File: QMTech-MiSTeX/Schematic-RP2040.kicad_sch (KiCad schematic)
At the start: 24 parts, among them J6 Conn_01x02, U3 W25Q128JVS, U4 RP2040, X1 X322512MSB4SI

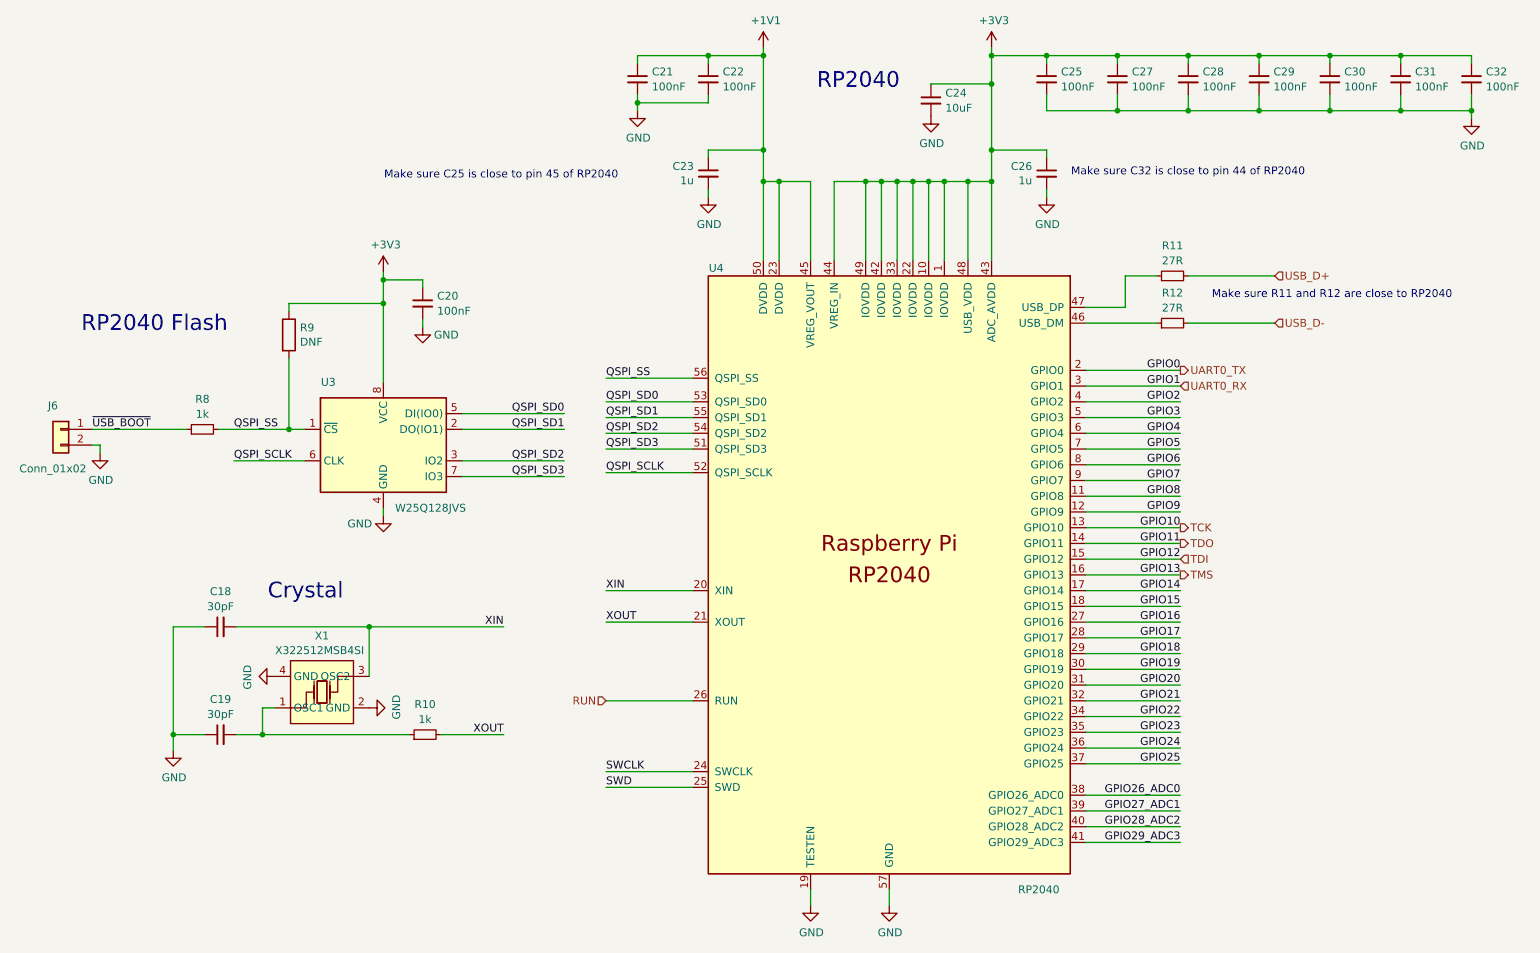
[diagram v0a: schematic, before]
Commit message: apply review notes from somhi, move audio into its own subsheet, add analog audio out
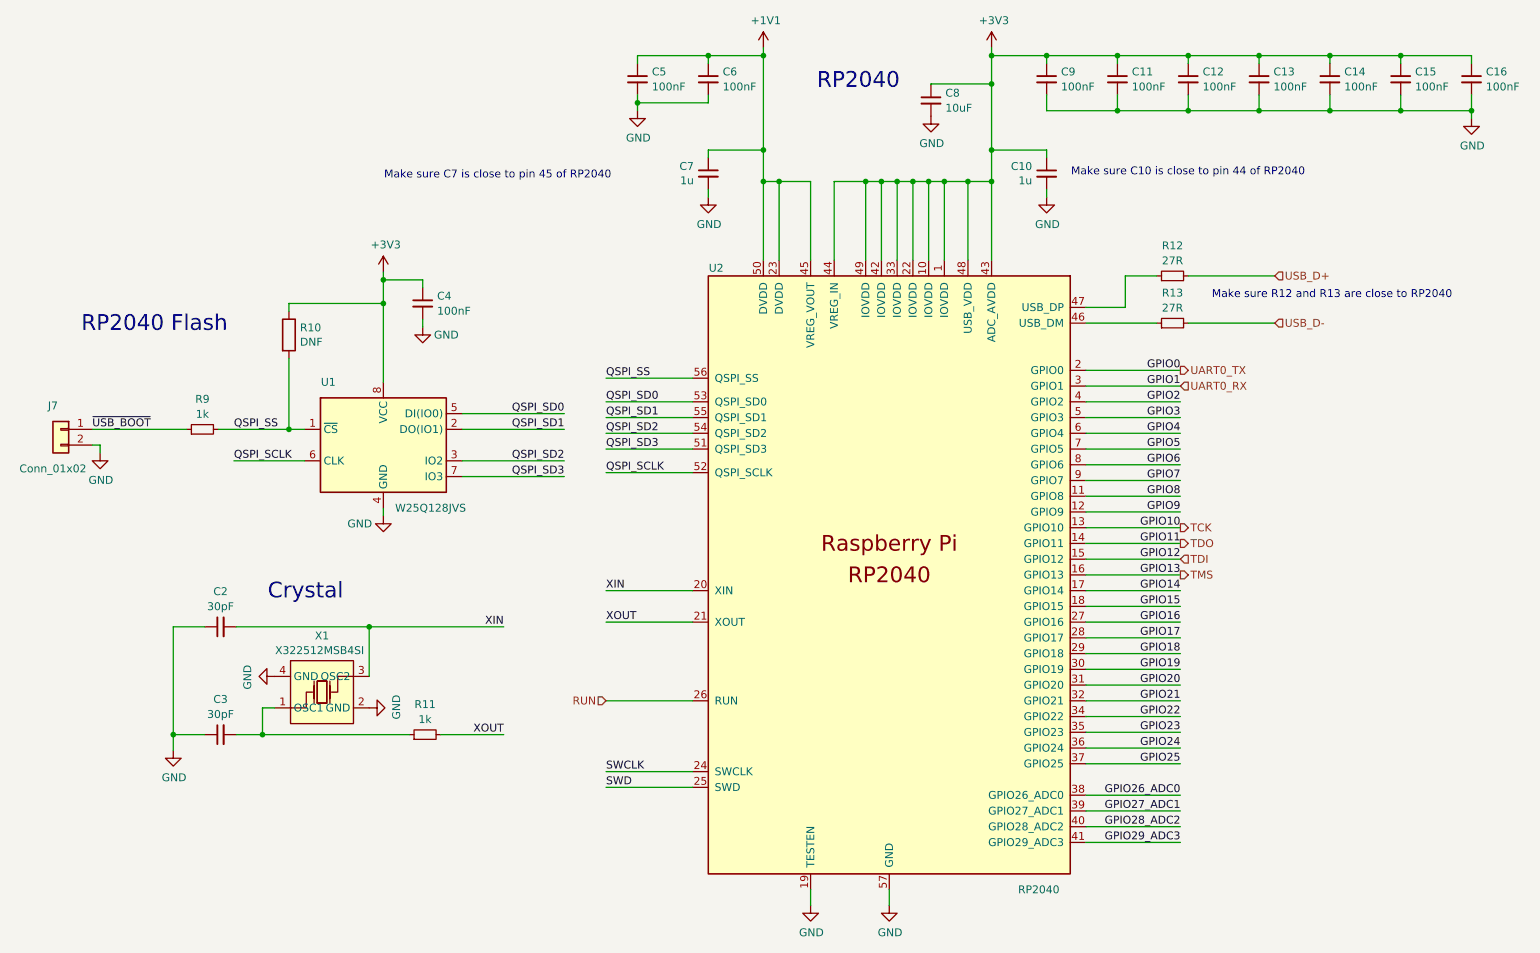
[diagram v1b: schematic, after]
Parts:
- renumbered C26 to C10, C27 to C11, C28 to C12, C29 to C13, C30 to C14, C31 to C15, C32 to C16, C18 to C2, C19 to C3, C20 to C4, C21 to C5, C22 to C6, C23 to C7, C24 to C8, C25 to C9, J6 to J7, R9 to R10, R10 to R11, R11 to R12, R12 to R13, R8 to R9, U3 to U1, U4 to U2
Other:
- note added: "Make sure C10 is close to pin 44 of RP2040"
- note added: "Make sure C7 is close to pin 45 of RP2040"
- note added: "Make sure R12 and R13 are close to RP2040"
- note removed: "Make sure C25 is close to pin 45 of RP2040"
- note removed: "Make sure C32 is close to pin 44 of RP2040"
- note removed: "Make sure R11 and R12 are close to RP2040"

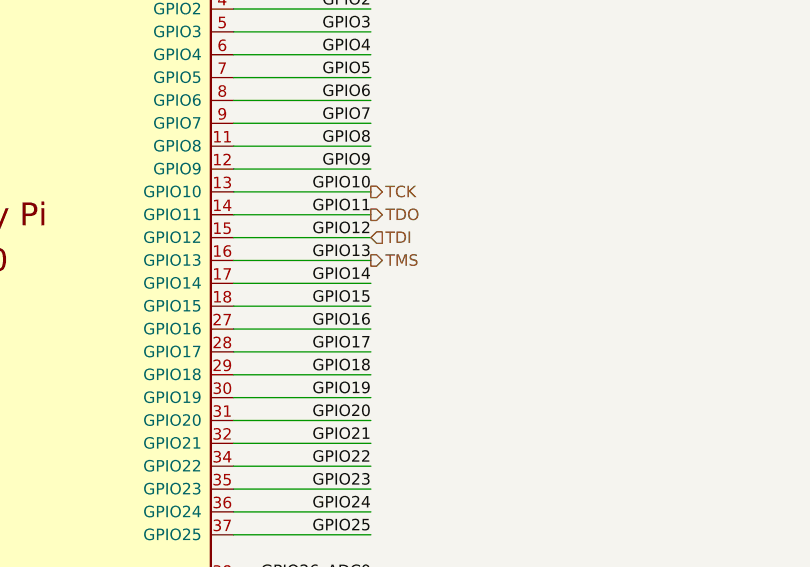
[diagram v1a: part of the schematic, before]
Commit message: add UART connections
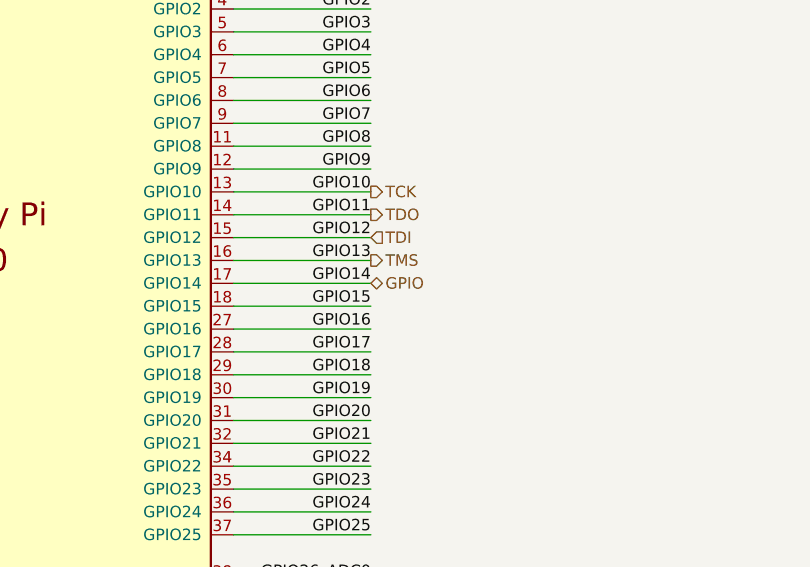
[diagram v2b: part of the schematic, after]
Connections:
- net GPIO14 renamed GPIO
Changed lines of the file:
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@@
     (effects (font (size 1.27 1.27)) (justify right))
+  )
+  (hierarchical_label "GPIO" (shape bidirectional) (at 201.6506 107.5182 0) (fields_autoplaced)
+    (effects (font (size 1.27 1.27)) (justify left))
   )
   (hierarchical_label "TMS" (shape output) (at 201.6506 104.9782 0) (fields_autoplaced)

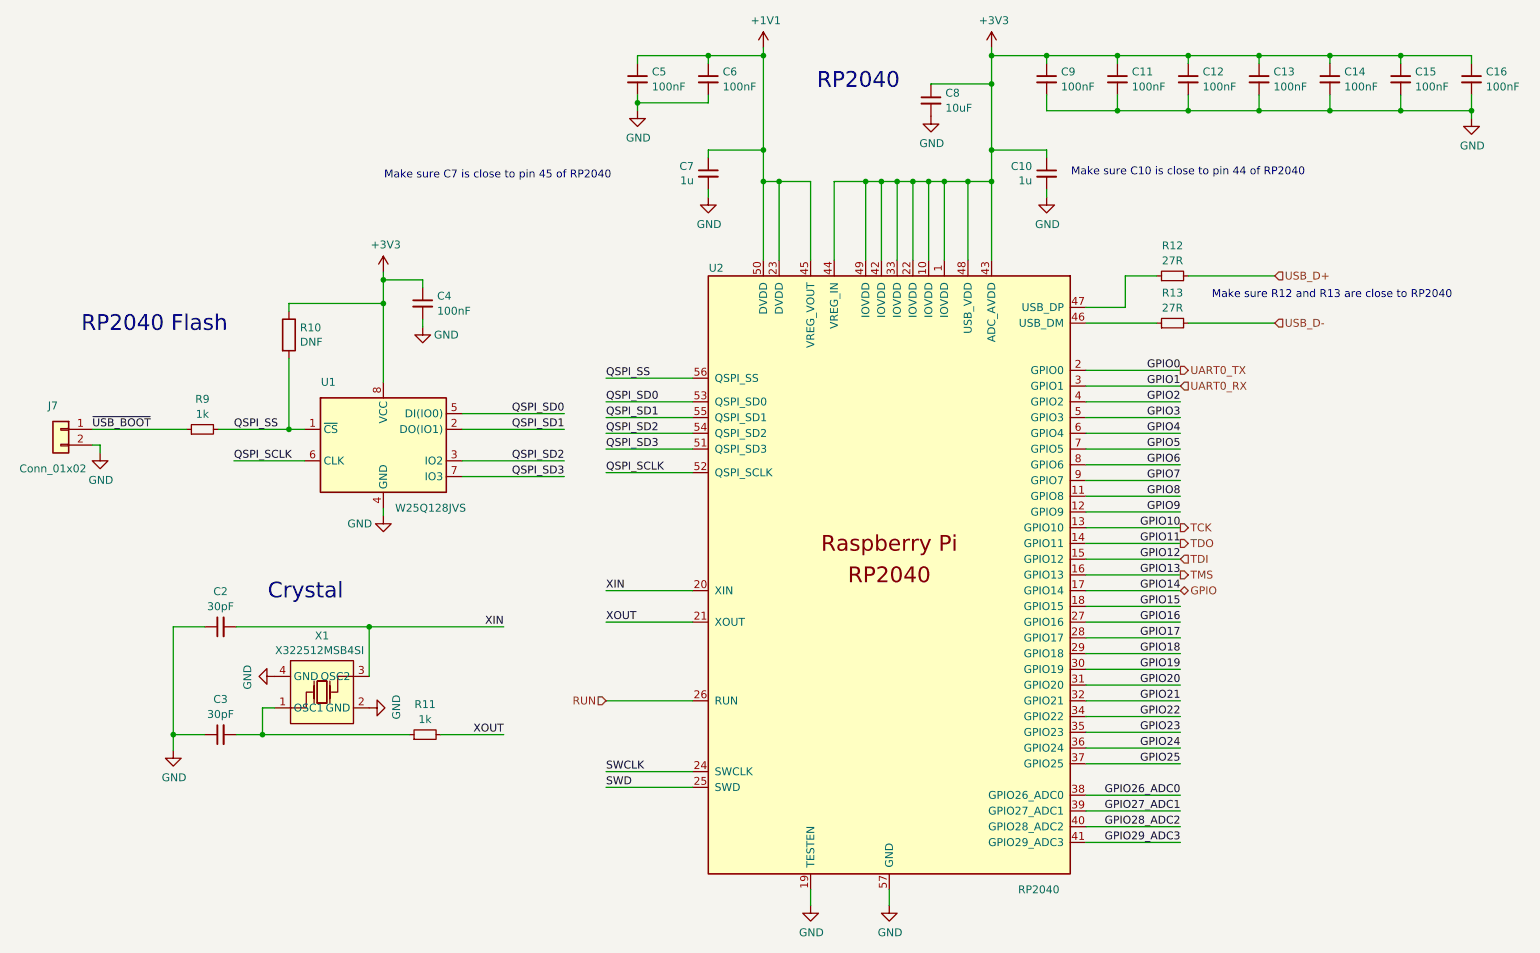
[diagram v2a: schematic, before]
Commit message: finish routing/layouting, fix silk screen, add mounting holes
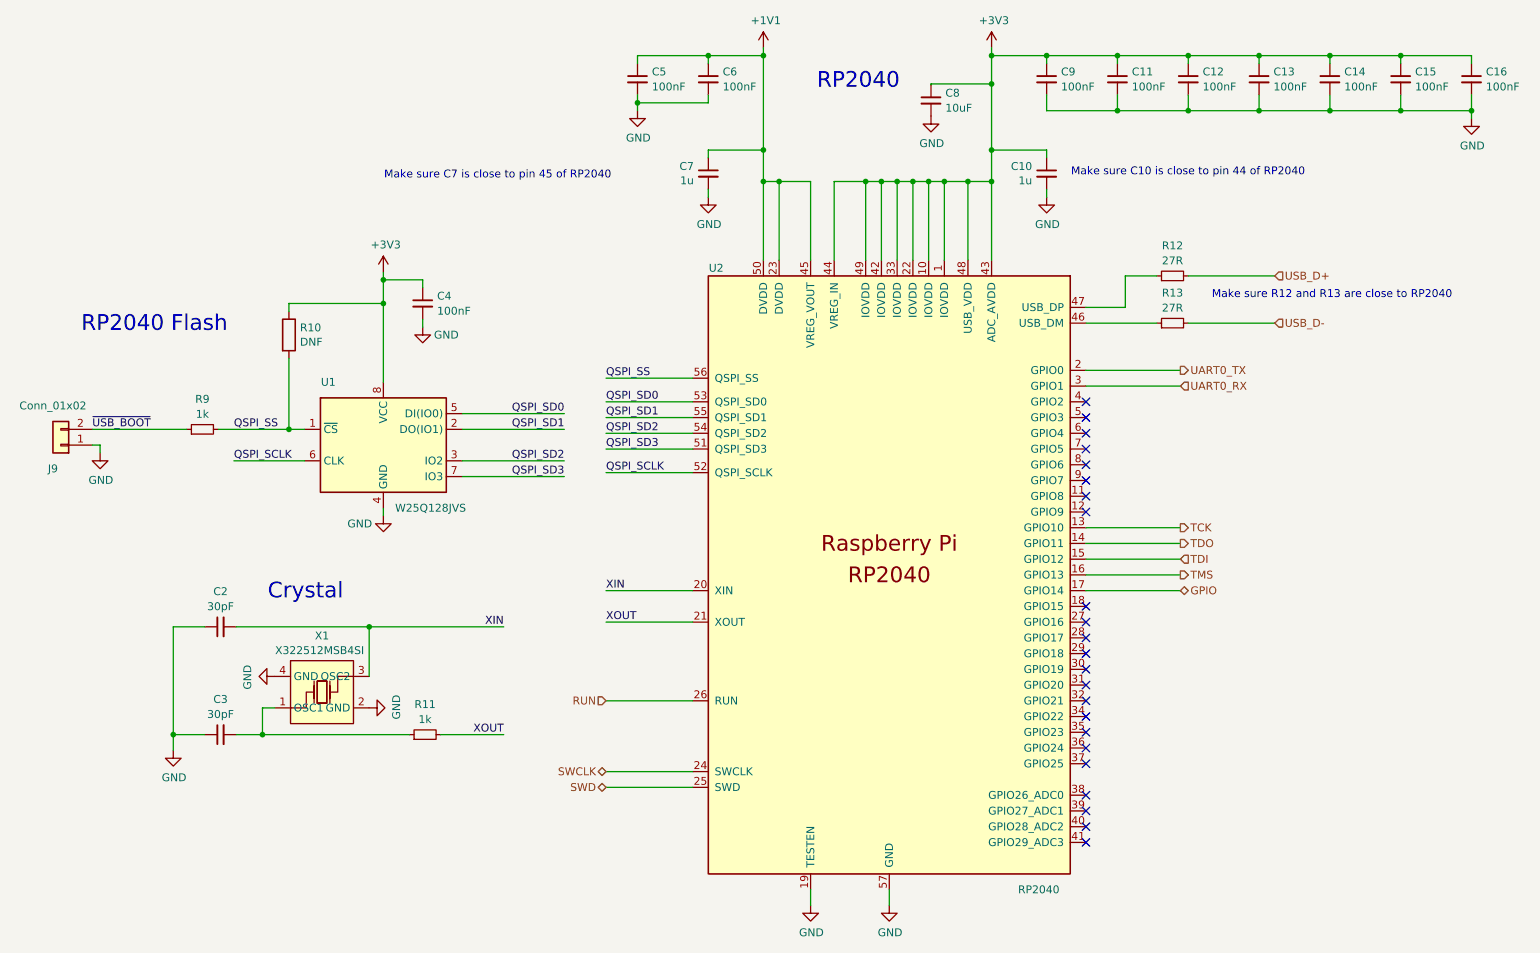
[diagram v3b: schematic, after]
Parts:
- U2: footprint RP2040_minimal:RP2040-QFN-56 -> easyeda2kicad:LQFN-56_L7.0-W7.0-P0.4-EP
- renumbered J7 to J9
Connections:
- net GND: now also J9.1 (Pin_1); no longer J9.2 (Pin_2)
- net ~{USB_BOOT}: now also J9.2 (Pin_2); no longer J9.1 (Pin_1)
- net GPIO15: no longer names the net of U2.18 (GPIO15)
- net GPIO16: no longer names the net of U2.27 (GPIO16)
- net GPIO17: no longer names the net of U2.28 (GPIO17)
- net GPIO18: no longer names the net of U2.29 (GPIO18)
- net GPIO19: no longer names the net of U2.30 (GPIO19)
- net GPIO2: no longer names the net of U2.4 (GPIO2)
- net GPIO20: no longer names the net of U2.31 (GPIO20)
- net GPIO21: no longer names the net of U2.32 (GPIO21)
- net GPIO22: no longer names the net of U2.34 (GPIO22)
- net GPIO23: no longer names the net of U2.35 (GPIO23)
- net GPIO24: no longer names the net of U2.36 (GPIO24)
- net GPIO25: no longer names the net of U2.37 (GPIO25)
- net GPIO26_ADC0: no longer names the net of U2.38 (GPIO26_ADC0)
- net GPIO27_ADC1: no longer names the net of U2.39 (GPIO27_ADC1)
- net GPIO28_ADC2: no longer names the net of U2.40 (GPIO28_ADC2)
- net GPIO29_ADC3: no longer names the net of U2.41 (GPIO29_ADC3)
- net GPIO3: no longer names the net of U2.5 (GPIO3)
- net GPIO4: no longer names the net of U2.6 (GPIO4)
- net GPIO5: no longer names the net of U2.7 (GPIO5)
- net GPIO6: no longer names the net of U2.8 (GPIO6)
- net GPIO7: no longer names the net of U2.9 (GPIO7)
- net GPIO8: no longer names the net of U2.11 (GPIO8)
- net GPIO9: no longer names the net of U2.12 (GPIO9)
- no-connect marks 0 -> 23
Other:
- moved on the sheet: J9
